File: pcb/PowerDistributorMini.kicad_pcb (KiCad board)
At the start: 2 copper layers, 104 x 29 mm, 23 parts, among them J1 F1, J10 D2, J11 D3, J12 D4, J13 D5, J14 D6, J15 D7, J16 D8, J17 PWR, J2 F2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

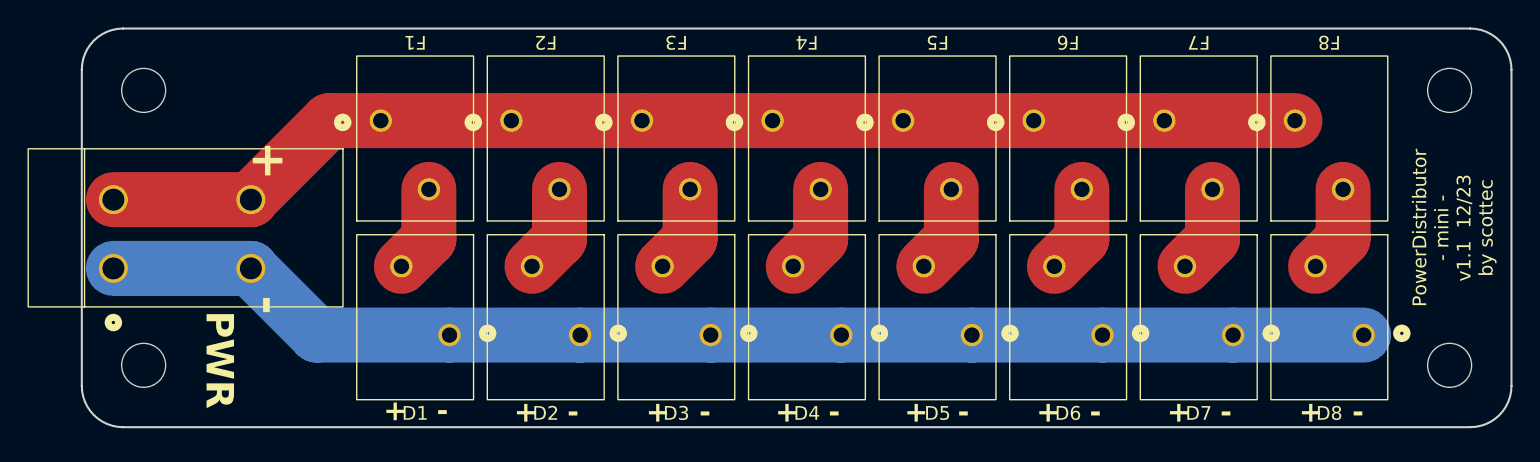
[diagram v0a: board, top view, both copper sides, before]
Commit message: v1.2 : alterative main connector; some markings
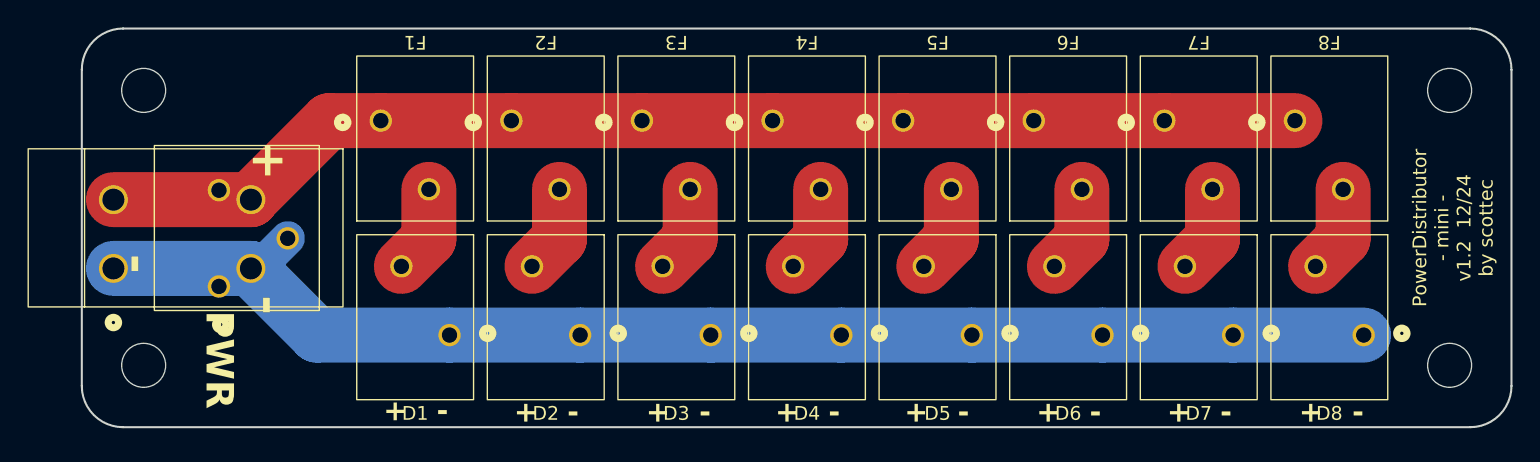
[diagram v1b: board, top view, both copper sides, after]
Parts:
- removed the REF** at (172.1, 104.9)
- added J18: PWR, GSI_footprints:Wago-250-203, F.Cu at (93.3, 99.2)
- added REF**: OSHW-Symbol_6.7x6mm_SilkScreen, Symbol:OSHW-Symbol_6.7x6mm_SilkScreen, B.Cu at (90.8, 95.4)
- moved REF** 79.1 mm to (176.9, 95.1)
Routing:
- net GND: track 93.0 -> 96.6 mm
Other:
- board text added: "-"
- board text added: "PowerDistributor - mini - v1.2 12/24 by scottec"
- board text added: "https://github.com/SoaringCircuits/PowerDistributorMini"
- board text removed: "M3"
- board text removed: "PowerDistributor - mini - v1.1 12/23 by scottec"
